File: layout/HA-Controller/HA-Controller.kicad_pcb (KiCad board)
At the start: 2 copper layers, 124.5 x 99.1 mm, 62 parts, among them J1 Conn_01x03, J2 Conn_01x06, J3 Conn_01x08, J4 Conn_01x10, J5 Conn_01x08, J6 Conn_01x15, J7 Conn_01x15, J8 Conn_01x04, J9 Conn_01x04, K1 FINDER-44.62, K2 FINDER-44.62, M1 Jumper, M2 Jumper, Q1 BC547, Q2 BC547, U1 ESP-12E, U2 IRM-15-24, U3 TSR_1-2450

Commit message: Layout abgespeckt
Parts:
- removed C4, C6, C8: 100n, Capacitor_SMD:C_0603_1608Metric
- removed C7: 10uF/50V, Capacitor_THT:CP_Radial_D6.3mm_P2.50mm
- removed D1: 1N4148, Diode_THT:D_DO-35_SOD27_P7.62mm_Horizontal
- removed D3, D6: LED_Small, LED_THT:LED_D3.0mm
- removed F1: 0,1A, Fuse:Fuseholder_Cylinder-5x20mm_Stelvio-Kontek_PTF78_Horizontal_Open
- removed J1: Conn_01x03, Connector_Phoenix_MSTB:PhoenixContact_MSTBA_2,5_3-G-5,08_1x03_P5.08mm_Horizontal
- removed J3, J5: Conn_01x08, Connector_PinSocket_2.54mm:PinSocket_1x08_P2.54mm_Vertical
- removed JP1: Jumper_NC_Small, Connector_PinHeader_2.54mm:PinHeader_1x02_P2.54mm_Vertical
- removed K2: FINDER-44.62, Relay_THT:Relay_DPDT_Finder_40.52
- removed M1: Jumper, kp-Bom_only:Jumper
- removed Q1: BC547, Package_TO_SOT_THT:TO-92_Inline
- removed R1: 4K7, Resistor_THT:R_Axial_DIN0309_L9.0mm_D3.2mm_P12.70mm_Horizontal
- removed R15, R9: 1K5, Resistor_THT:R_Axial_DIN0309_L9.0mm_D3.2mm_P12.70mm_Horizontal
- removed R2: 470, Resistor_THT:R_Axial_DIN0309_L9.0mm_D3.2mm_P12.70mm_Horizontal
- removed R4: 1K2, Resistor_THT:R_Axial_DIN0309_L9.0mm_D3.2mm_P12.70mm_Horizontal
- removed R5: 0, Resistor_THT:R_Axial_DIN0309_L9.0mm_D3.2mm_P12.70mm_Horizontal
- removed R6: 2K2, Resistor_THT:R_Axial_DIN0309_L9.0mm_D3.2mm_P12.70mm_Horizontal
- removed RV2: 24V, Varistor:RV_Disc_D7mm_W3.4mm_P5mm
- removed U1: ESP-12E, RF_Module:ESP-12E
- removed U2: IRM-15-24, Zielke:NT-Meanwell-IRM-15
- removed U3: TSR_1-2450, Converter_DCDC:Converter_DCDC_TRACO_TSR-1_THT
- moved D4 14.8 mm to (154.9, 104.1), turned to 270 degrees
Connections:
- net /SWPumpOff renamed /SW_Reserved
- D2 pad 1: +24V -> +5V
- J2 pad 1: /K2-12 -> +5V
- J2 pad 2: /K2-14 -> GND
- J2 pad 3: /K2-11 -> Net-(J2-Pad3)
- J4 pad 2: /Level -> Net-(J4-Pad2)
- J4 pad 4: /SWMaxNC -> /GPIO12
- J4 pad 5: +24V -> +5V
- J6 pad 1: /ADC -> Net-(J6-Pad1)
- K1 pad A1: +24V -> +5V
- R10 pad 1: +24V -> +5V
- RV1 pad 1: /SWMaxNC -> /GPIO12
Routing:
- net +24V: track 204.5 -> 0.00 mm, vias 3 -> 0
- net +5V: track 268.9 -> 434.0 mm, vias 11 -> 14
- net /ADC: track 85.9 -> 0.00 mm
- net /GPIO2: track 109.8 -> 48.3 mm, vias 1 -> 0
- net /GPIO16: track 94.3 -> 44.8 mm, vias 2 -> 1
- net /RST: track 48.7 -> 0.00 mm
- net /GPIO14: track 79.8 -> 31.5 mm, vias 5 -> 3
- net /GPIO13: track 60.0 -> 12.7 mm, vias 1 -> 0
- net /SWMaxNC: track 45.7 -> 0.00 mm
- net /EN: track 44.2 -> 0.00 mm
- net Net-(D1-Pad2): track 43.2 -> 0.00 mm
- net Net-(Q1-Pad2): track 41.2 -> 0.00 mm, vias 2 -> 0
- net /K2-12: track 30.6 -> 0.00 mm
- net Net-(J1-Pad2): track 25.6 -> 0.00 mm
- net /K2-11: track 24.5 -> 0.00 mm
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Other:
- board text removed: "K2_11"
- board text removed: "K2_12"
- board text removed: "K2_14"
- board text removed: "L1"
- board text removed: "Lev"
- board text removed: "N"
- board text removed: "PE"
- board text removed: "Pump"

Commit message: Layout abgespeckt
Signed-off-by: Claus Zielke <info@cszielke.de>
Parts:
- removed R13: 1K, Resistor_THT:R_Axial_DIN0309_L9.0mm_D3.2mm_P12.70mm_Horizontal
- removed RV1, RV3, RV4: 24V, Varistor:RV_Disc_D7mm_W3.4mm_P5mm
- J4: value Conn_01x10 -> Conn_01x06; footprint Connector_Phoenix_MSTB:PhoenixContact_MSTBA_2,5_10-G-5,08_1x10_P5.08mm_Horizontal -> Connector_Phoenix_MSTB:PhoenixContact_MSTBA_2,5_6-G-5,08_1x06_P5.08mm_Horizontal
- K1: value FINDER-44.62 -> G5V-2; footprint Relay_THT:Relay_DPDT_Finder_40.52 -> Relay_THT:Relay_DPDT_Omron_G5V-2
- R11: value 47K -> 3K3
- moved C5 73.7 mm to (174.0, 66.0), turned to 0 degrees
- moved C3 73.3 mm to (172.8, 68.6), turned to 0 degrees
- moved R14 65.3 mm to (177.8, 76.2), turned to 180 degrees
- moved D5 59.3 mm to (177.8, 83.8)
- moved C1 52.1 mm to (86.4, 137.2)
- moved J8 30.7 mm to (86.4, 99.1), turned to 270 degrees
- moved JP2 27.4 mm to (94.0, 99.1)
- moved M2 27.4 mm to (94.0, 95.2)
- moved R7 26.2 mm to (99.1, 104.1), turned to 90 degrees
- moved R8 25.1 mm to (104.1, 104.1), turned to 90 degrees
- moved R16 20.7 mm to (124.5, 119.4), turned to 0 degrees
- moved R10 17.0 mm to (157.5, 91.4)
- moved J9 11.4 mm to (149.9, 124.5), turned to 270 degrees
- moved J4 10.2 mm to (129.5, 61.0)
- moved D2 8.03 mm to (152.4, 96.5), turned to 180 degrees
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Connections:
- J4 pad 2: Net-(J4-Pad2) -> /GPIO12
- J4 pad 3: +5V -> /SW_Reserved
- J4 pad 4: /GPIO12 -> +5V
- J4 pad 5: +5V -> Net-(J4-Pad5)
- J4 pad 6: /SW_Reserved -> Net-(J4-Pad6)
- K1 pad 11: /K1-11 -> /K1-12
- R12 pad 2: Net-(R12-Pad2) -> GND
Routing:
- net +5V: track 434.0 -> 328.7 mm, vias 14 -> 6
- net VCC: track 165.1 -> 215.9 mm, vias 8 -> 2
- net /GPIO5_CLK: track 85.9 -> 39.4 mm
- net /GPIO4_DAT: track 89.5 -> 44.5 mm
- net GND: track 389.8 -> 360.7 mm, vias 5 -> 2
- net /GPIO16: track 44.8 -> 17.3 mm, vias 1 -> 0
- net /K1-11: track 24.5 -> 38.1 mm
- net /GPIO12: track 96.5 -> 83.8 mm
- net /VI2C: track 22.9 -> 10.2 mm
- net Net-(D2-Pad2): track 43.2 -> 31.5 mm
- net /GPIO2: track 48.3 -> 37.2 mm, vias 0 -> 3
- net /SW_Reserved: track 108.3 -> 98.5 mm, vias 6 -> 1
- net Net-(J9-Pad3): track 10.2 -> 17.8 mm
- net Net-(R12-Pad2): track 5.08 -> 0.00 mm
- net /K1-14: track 15.6 -> 20.3 mm
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
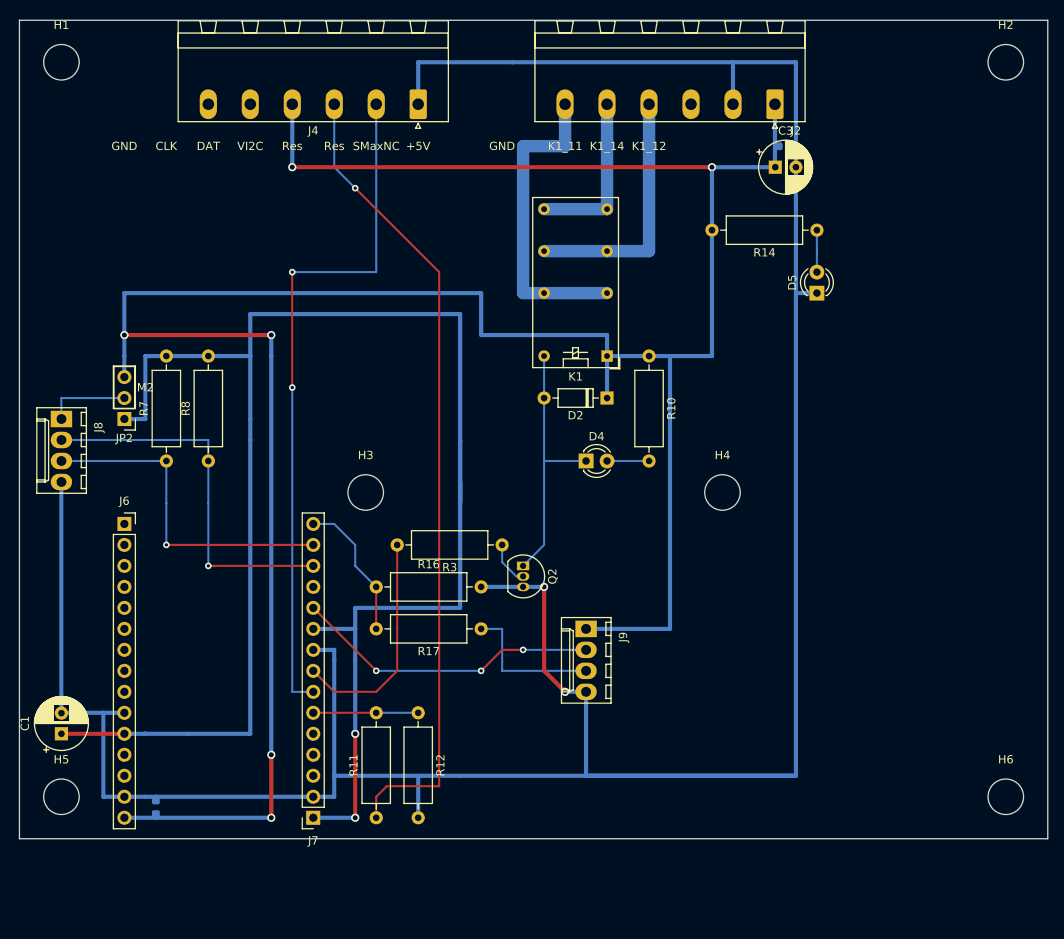
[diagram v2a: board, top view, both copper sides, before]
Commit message: Layout für Verteilerdose und Lochraster optimiert
Signed-off-by: Claus Zielke <info@cszielke.de>
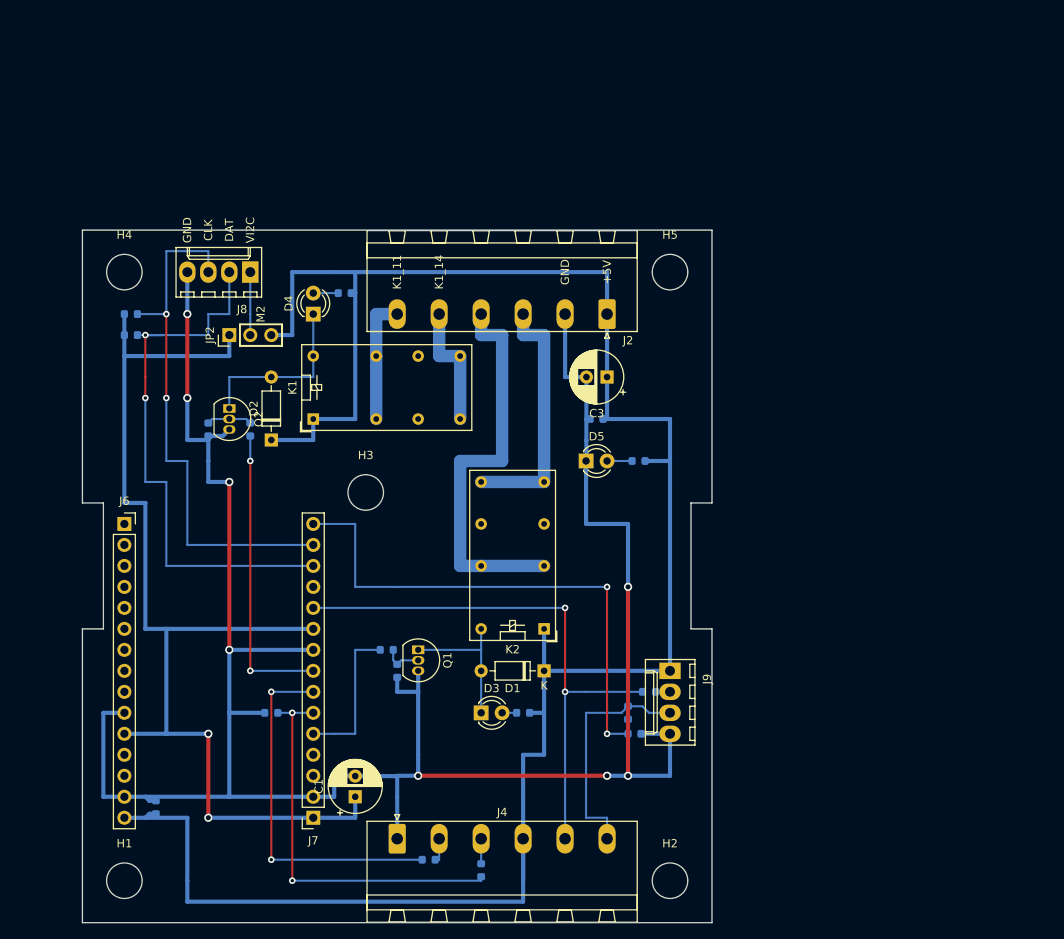
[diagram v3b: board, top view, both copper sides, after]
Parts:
- removed H6: MountingHole, MountingHole:MountingHole_4.3mm_M4_ISO14580
- added D1: 1N4148, Diode_THT:D_DO-35_SOD27_P7.62mm_Horizontal, F.Cu at (144.8, 129.5)
- added D3: LED_Small, LED_THT:LED_D3.0mm, F.Cu at (137.2, 134.6)
- added K2: G5V-2, Relay_THT:Relay_DPDT_Omron_G5V-2, F.Cu at (144.8, 124.5)
- added Q1: BC547, Package_TO_SOT_THT:TO-92_Inline, F.Cu at (129.5, 127.0)
- added R1: 330, Resistor_SMD:R_0603_1608Metric, B.Cu at (125.7, 127.0)
- added R2: 1K5, Resistor_SMD:R_0603_1608Metric, B.Cu at (142.2, 134.6)
- added R4: 100K, Resistor_SMD:R_0603_1608Metric, B.Cu at (127.0, 129.5)
- added R5: 100K, Resistor_SMD:R_0603_1608Metric, B.Cu at (104.1, 100.3)
- added R6: 4R7, Resistor_SMD:R_0603_1608Metric, B.Cu at (157.5, 132.1)
- added R9: 4R7, Resistor_SMD:R_0603_1608Metric, B.Cu at (130.8, 152.4)
- R10, R11, R12, R14, R16, R17, R3, R7, R8: footprint Resistor_THT:R_Axial_DIN0309_L9.0mm_D3.2mm_P12.70mm_Horizontal -> Resistor_SMD:R_0603_1608Metric; moved to B.Cu
- moved H2 107.1 mm to (160.0, 154.9)
- moved H1 99.4 mm to (94.0, 154.9)
- moved H5 97.3 mm to (160.0, 81.3)
- moved J4 88.9 mm to (127.0, 149.9), turned to 0 degrees
- moved H4 77.1 mm to (94.0, 81.3)
- moved D2 41.0 mm to (111.8, 101.6), turned to 90 degrees
- moved Q2 40.3 mm to (106.7, 97.8)
- moved C5 40.2 mm to (151.1, 99.1), turned to 180 degrees
- moved R10 37.6 mm to (120.7, 83.8), turned to 180 degrees
- moved D4 37.5 mm to (116.8, 86.4), turned to 90 degrees
- moved C1 36.4 mm to (121.9, 144.8)
- moved K1 36.4 mm to (116.8, 99.1), turned to 90 degrees
- moved R16 36.0 mm to (155.7, 137.2)
- moved R14 35.3 mm to (156.2, 104.1), turned to 0 degrees
- moved D5 34.5 mm to (149.9, 104.1), turned to 0 degrees
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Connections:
- J2 pad 3: Net-(J2-Pad3) -> /K2-14
- J2 pad 4: /K1-12 -> /K2-11
- J4 pad 2: /GPIO12 -> Net-(J4-Pad2)
- J4 pad 5: Net-(J4-Pad5) -> /GPIO2
- J4 pad 6: Net-(J4-Pad6) -> /Echo
- J7 pad 5: Net-(J7-Pad5) -> /GPIO15
- J9 pad 2: /GPIO2 -> Net-(J9-Pad2)
- J9 pad 3: Net-(J9-Pad3) -> /Echo
- K1 pad 11: /K1-12 -> Net-(K1-Pad11)
- K1 pad 6: /K1-12 -> Net-(K1-Pad6)
- R17 pad 1: Net-(J9-Pad3) -> /Echo
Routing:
- net /SW_Reserved: track 98.5 -> 3.02 mm, vias 1 -> 0
- net GND: track 360.7 -> 273.9 mm, vias 2 -> 8
- net VCC: track 215.9 -> 129.5 mm
- net +5V: track 328.7 -> 256.1 mm, vias 6 -> 0
- net /K2-11: track 0.00 -> 48.3 mm
- net /GPIO16: track 17.3 -> 65.3 mm, vias 0 -> 2
- net /GPIO12: track 83.8 -> 43.7 mm
- net /GPIO13: track 12.7 -> 48.0 mm, vias 0 -> 2
- net /GPIO2: track 37.2 -> 67.8 mm, vias 3 -> 2
- net /K2-14: track 0.00 -> 30.5 mm
- net /K1-12: track 30.5 -> 0.00 mm
- net /Echo: track 0.00 -> 28.6 mm
- net /GPIO4_DAT: track 44.5 -> 71.1 mm, vias 1 -> 2
- net /GPIO5_CLK: track 39.4 -> 64.5 mm, vias 1 -> 2
- net /K1-11: track 38.1 -> 15.2 mm
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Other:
- board size 124.5 x 99.1 mm -> 76.2 x 83.8 mm
- board text removed: "K1_12"
- board text removed: "Res"
- board text removed: "SMaxNC"
